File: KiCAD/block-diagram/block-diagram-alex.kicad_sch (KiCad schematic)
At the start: 35 parts, among them J1 Conn_01x08, J2 Conn_01x08, J3 Conn_01x10, Q3 NMOS, Q4 NMOS, U1 74HC02, U3 74HC11, U6 LMC555xM

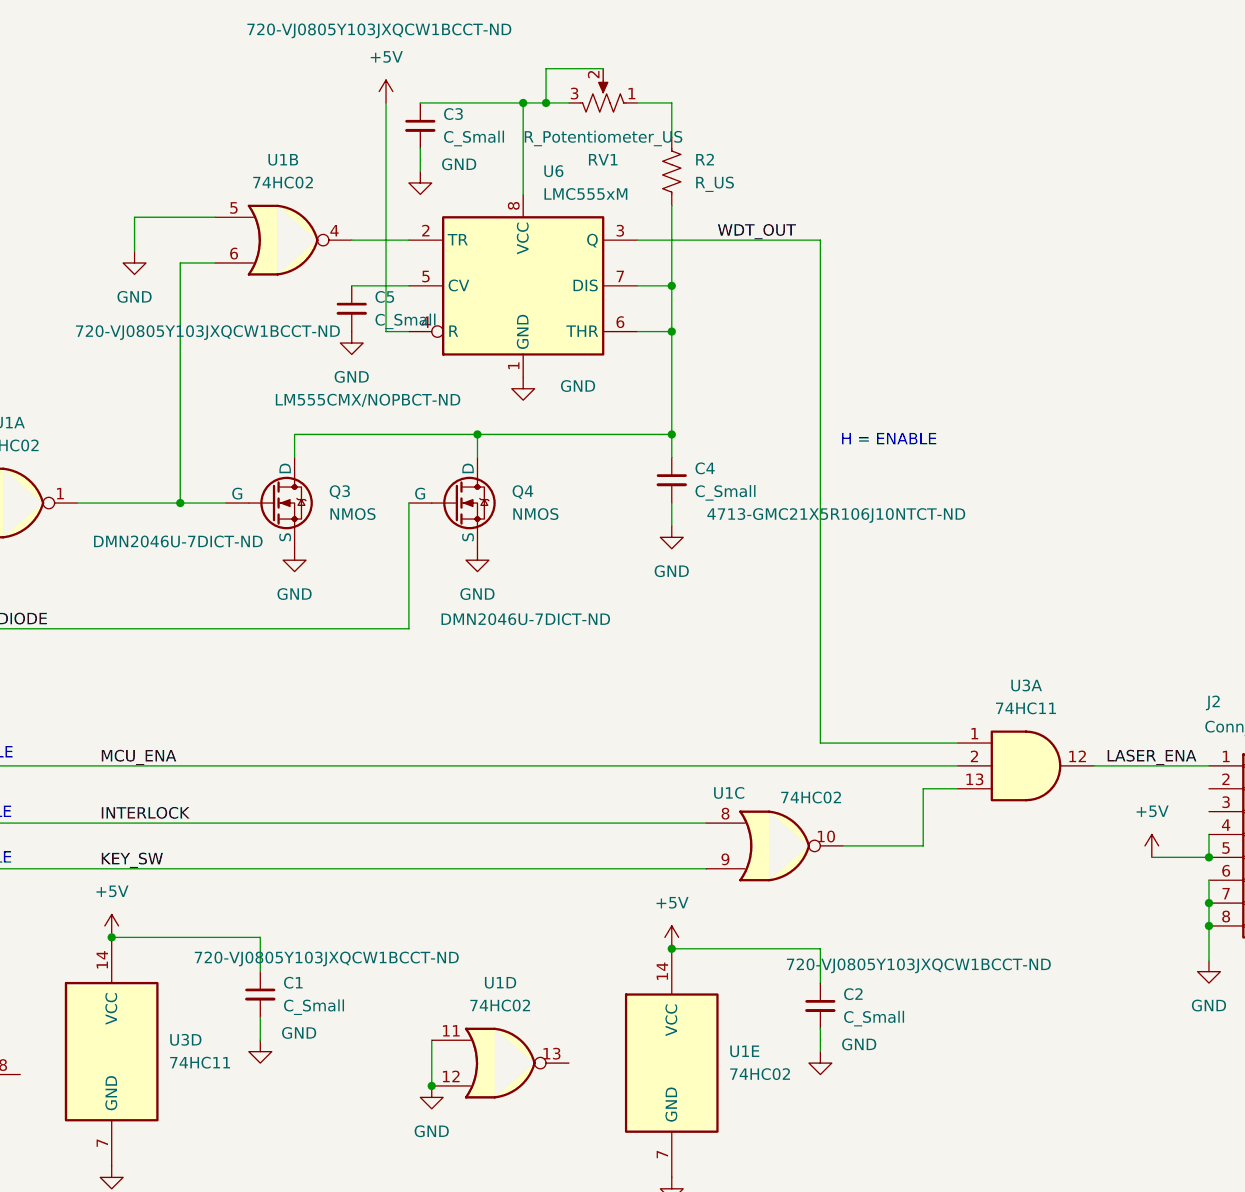
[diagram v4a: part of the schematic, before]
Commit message: Bypass Capacitor changes and Value Update
Changed all bypass capacitors to 0.1 uF and changed the value term to reflect capacitance.
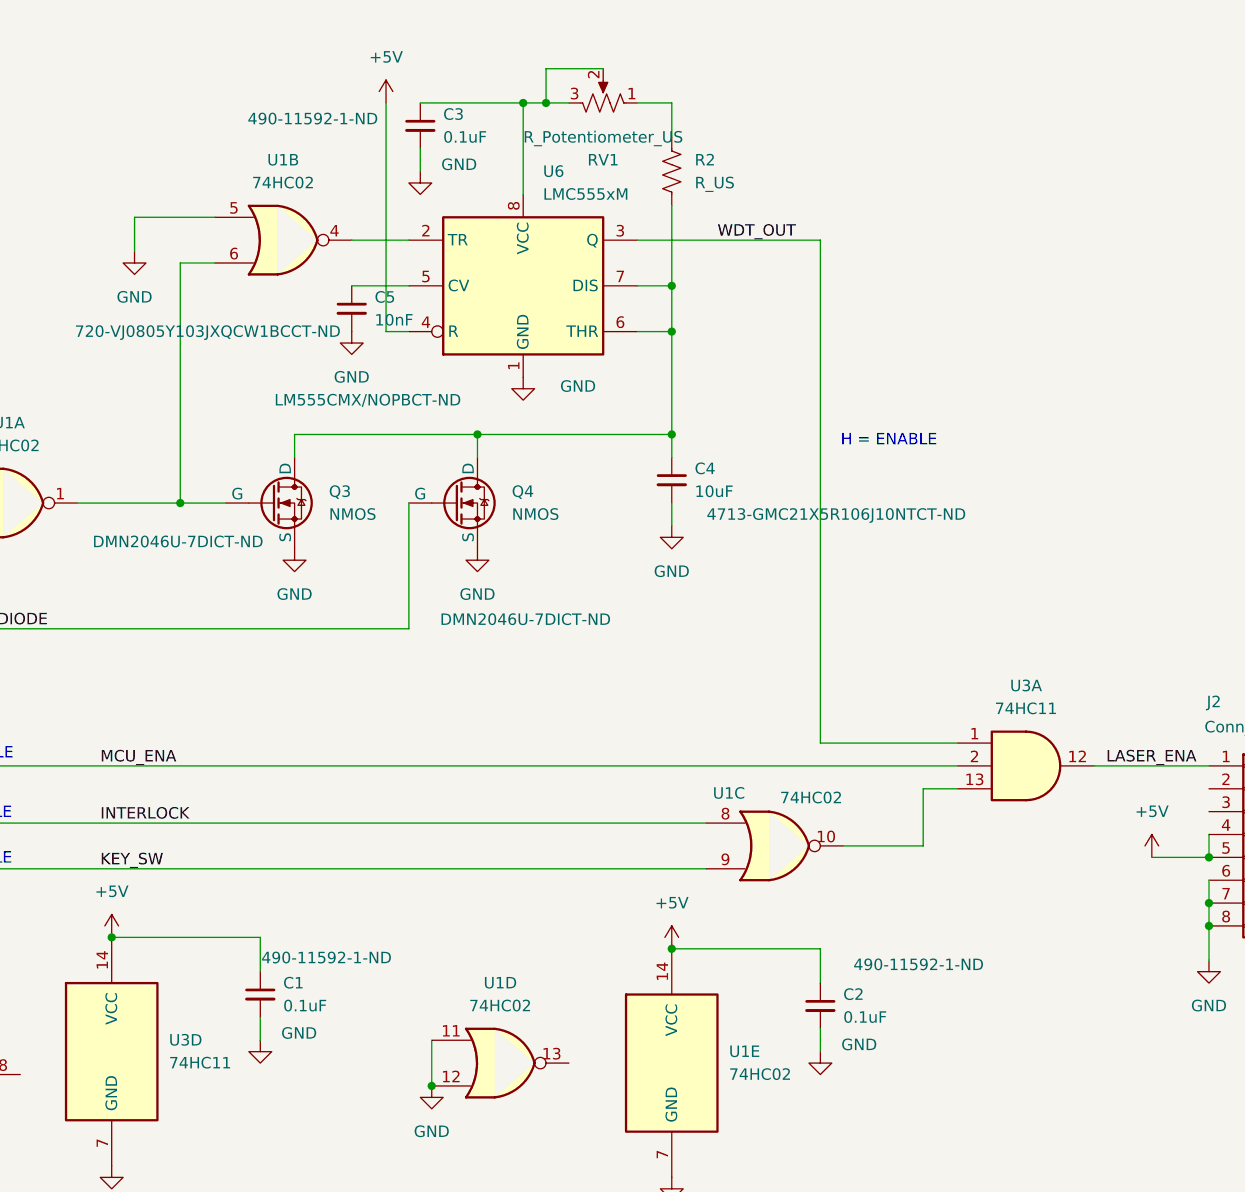
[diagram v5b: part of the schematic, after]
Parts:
- C1, C2, C3: value C_Small -> 0.1uF; CatNo 720-VJ0805Y103JXQCW1BCCT-ND -> 490-11592-1-ND; MfgNo VJ0805Y103JXQCW1BC -> GRM21B7U1A104JA01L
- C4: value C_Small -> 10uF
- C5: value C_Small -> 10nF
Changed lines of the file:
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@@
 			)
 		)
-		(property "Value" "C_Small"
+		(property "Value" "0.1uF"
 			(at 168.91 123.1962 0)
 			(effects
@@
 			)
 		)
-		(property "CatNo" "720-VJ0805Y103JXQCW1BCCT-ND"
+		(property "CatNo" "490-11592-1-ND"
 			(at 173.736 117.856 0)
 			(effects
@@
 			)
 		)
-		(property "MfgNo" "VJ0805Y103JXQCW1BC"
+		(property "MfgNo" "GRM21B7U1A104JA01L"
 			(at 166.37 121.92 0)
 			(effects
@@
 			)
 		)
-		(property "Value" "C_Small"
+		(property "Value" "0.1uF"
 			(at 186.69 26.6762 0)
 			(effects
@@
 			)
 		)
-		(property "CatNo" "720-VJ0805Y103JXQCW1BCCT-ND"
-			(at 179.578 14.732 0)
-			(effects
-				(font
-					(size 1.27 1.27)
-				)
-			)
-		)
-		(property "MfgNo" "VJ0805Y103JXQCW1BC"
+		(property "CatNo" "490-11592-1-ND"
+			(at 172.212 24.638 0)
+			(effects
+				(font
+					(size 1.27 1.27)
+				)
+			)
+		)
+		(property "MfgNo" "GRM21B7U1A104JA01L"
 			(at 184.15 25.4 0)
 			(effects
@@
 			)
 		)
-		(property "Value" "C_Small"
+		(property "Value" "10nF"
 			(at 179.07 46.9962 0)
 			(effects
@@
 			)
 		)
-		(property "Value" "C_Small"
+		(property "Value" "0.1uF"
 			(at 231.14 124.4662 0)
 			(effects
@@
 			)
 		)
-		(property "CatNo" "720-VJ0805Y103JXQCW1BCCT-ND"
+		(property "CatNo" "490-11592-1-ND"
 			(at 239.522 118.618 0)
 			(effects
@@
 			)
 		)
-		(property "MfgNo" "VJ0805Y103JXQCW1BC"
+		(property "MfgNo" "GRM21B7U1A104JA01L"
 			(at 228.6 123.19 0)
 			(effects
@@
 			)
 		)
-		(property "Value" "C_Small"
+		(property "Value" "10uF"
 			(at 214.63 66.0462 0)
 			(effects

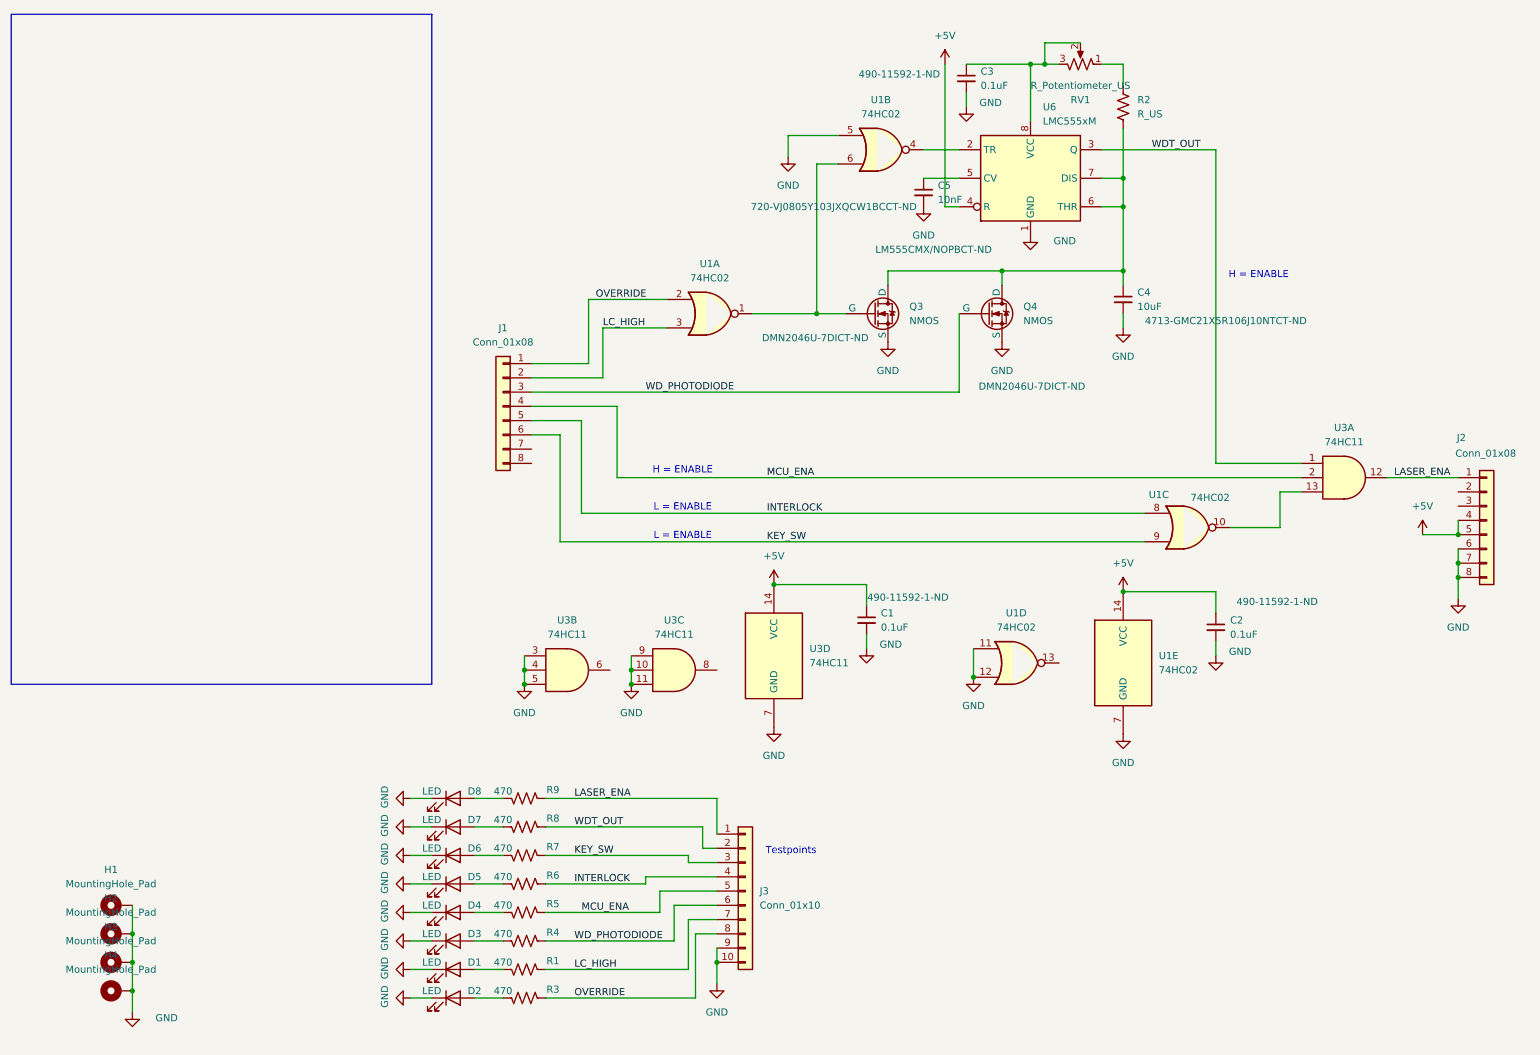
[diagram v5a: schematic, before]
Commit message: Logic Gate CatNo and MfgNo
Added part and manufacturer numbers for the logic gates.
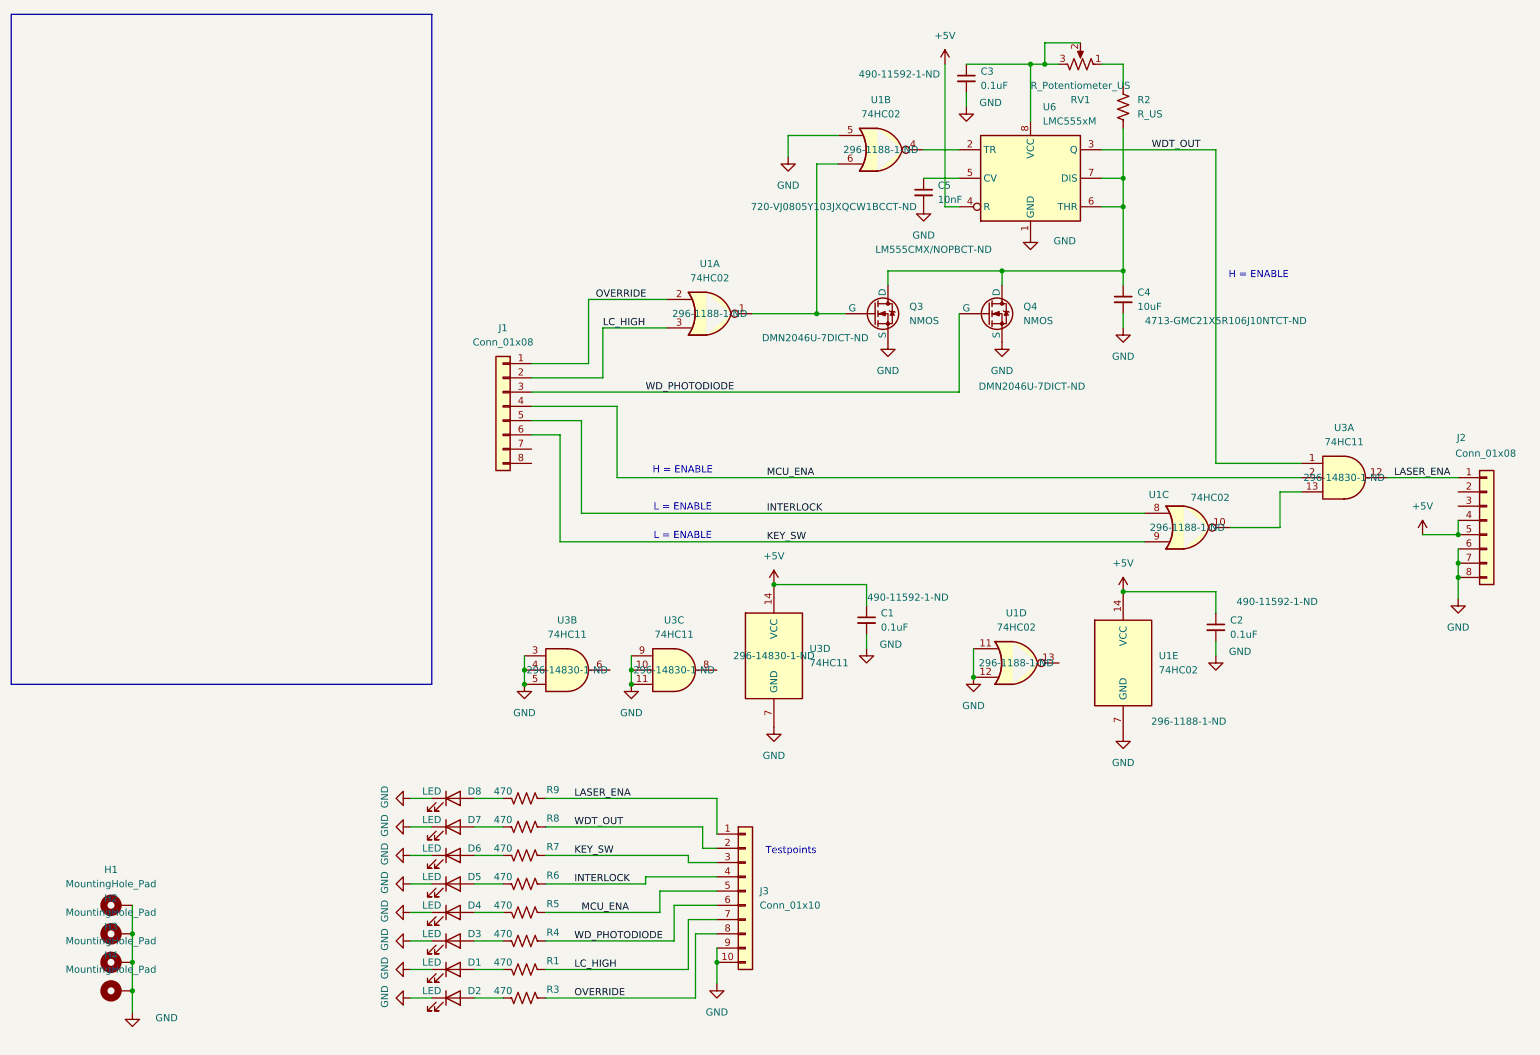
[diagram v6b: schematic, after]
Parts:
- U1: CatNo (none) -> 296-1188-1-ND; MfgNo (none) -> SN74HC02DR
- U3: CatNo (none) -> 296-14830-1-ND; MfgNo (none) -> SN74HC11DR
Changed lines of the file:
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@@
 			)
 		)
+		(property "CatNo" "296-1188-1-ND"
+			(at 168.91 38.1 0)
+			(effects
+				(font
+					(size 1.27 1.27)
+				)
+			)
+		)
+		(property "MfgNo" "SN74HC02DR"
+			(at 168.91 38.1 0)
+			(effects
+				(font
+					(size 1.27 1.27)
+				)
+				(hide yes)
+			)
+		)
 		(pin "10"
 		)
@@
 			)
 		)
+		(property "CatNo" "296-1188-1-ND"
+			(at 223.52 105.41 0)
+			(effects
+				(font
+					(size 1.27 1.27)
+				)
+			)
+		)
+		(property "MfgNo" "SN74HC02DR"
+			(at 223.52 105.41 0)
+			(effects
+				(font
+					(size 1.27 1.27)
+				)
+				(hide yes)
+			)
+		)
 		(pin "10"
 		)
@@
 			)
 		)
+		(property "CatNo" "296-1188-1-ND"
+			(at 138.43 67.31 0)
+			(effects
+				(font
+					(size 1.27 1.27)
+				)
+			)
+		)
+		(property "MfgNo" "SN74HC02DR"
+			(at 138.43 67.31 0)
+			(effects
+				(font
+					(size 1.27 1.27)
+				)
+				(hide yes)
+			)
+		)
 		(pin "10"
 		)
@@
 			)
 		)
+		(property "CatNo" "296-14830-1-ND"
+			(at 132.08 130.81 0)
+			(effects
+				(font
+					(size 1.27 1.27)
+				)
+			)
+		)
+		(property "MfgNo" "SN74HC11DR"
+			(at 132.08 130.81 0)
+			(effects
+				(font
+					(size 1.27 1.27)
+				)
+				(hide yes)
+			)
+		)
 		(pin "11"
 		)
@@
 			)
 		)
+		(property "CatNo" "296-1188-1-ND"
+			(at 193.04 129.54 0)
+			(effects
+				(font
+					(size 1.27 1.27)
+				)
+			)
+		)
+		(property "MfgNo" "SN74HC02DR"
+			(at 193.04 129.54 0)
+			(effects
+				(font
+					(size 1.27 1.27)
+				)
+				(hide yes)
+			)
+		)
 		(pin "11"
 		)
@@
 		(on_board yes)
 		(dnp no)
-		(fields_autoplaced yes)
 		(property "Reference" "U1"
 			(at 218.44 128.2699 0)
@@
 			)
 		)
+		(property "CatNo" "296-1188-1-ND"
+			(at 223.774 139.954 0)
+			(effects
+				(font
+					(size 1.27 1.27)
+				)
+			)
+		)
+		(property "MfgNo" "SN74HC02DR"
+			(at 212.09 129.54 0)
+			(effects
+				(font
+					(size 1.27 1.27)
+				)
+				(hide yes)
+			)
+		)
 		(pin "11"
 		)
@@
 			)
 		)
+		(property "CatNo" "296-14830-1-ND"
+			(at 251.46 96.52 0)
+			(effects
+				(font
+					(size 1.27 1.27)
+				)
+			)
+		)
+		(property "MfgNo" "SN74HC11DR"
+			(at 251.46 96.52 0)
+			(effects
+				(font
+					(size 1.27 1.27)
+				)
+				(hide yes)
+			)
+		)
 		(pin "7"
 		)
@@
 			)
 		)
+		(property "CatNo" "296-14830-1-ND"
+			(at 113.03 130.81 0)
+			(effects
+				(font
+					(size 1.27 1.27)
+				)
+			)
+		)
+		(property "MfgNo" "SN74HC11DR"
+			(at 113.03 130.81 0)
+			(effects
+				(font
+					(size 1.27 1.27)
+				)
+				(hide yes)
+			)
+		)
 		(pin "7"
 		)
@@
 			(at 149.86 128.27 0)
 			(effects
+				(font
+					(size 1.27 1.27)
+				)
+				(hide yes)
+			)
+		)
+		(property "CatNo" "296-14830-1-ND"
+			(at 149.86 128.27 0)
+			(effects
+				(font
+					(size 1.27 1.27)
+				)
+			)
+		)
+		(property "MfgNo" "SN74HC11DR"
+			(at 149.86 128.27 0)
+			(effects
